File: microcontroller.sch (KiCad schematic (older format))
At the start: 12 parts

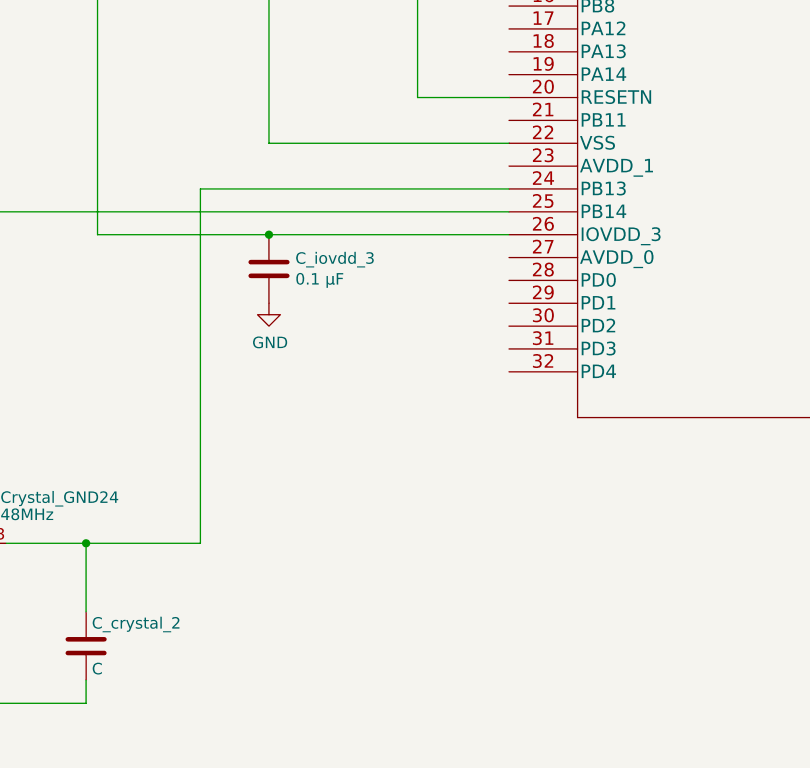
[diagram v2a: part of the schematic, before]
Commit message: Add avdd capacitors
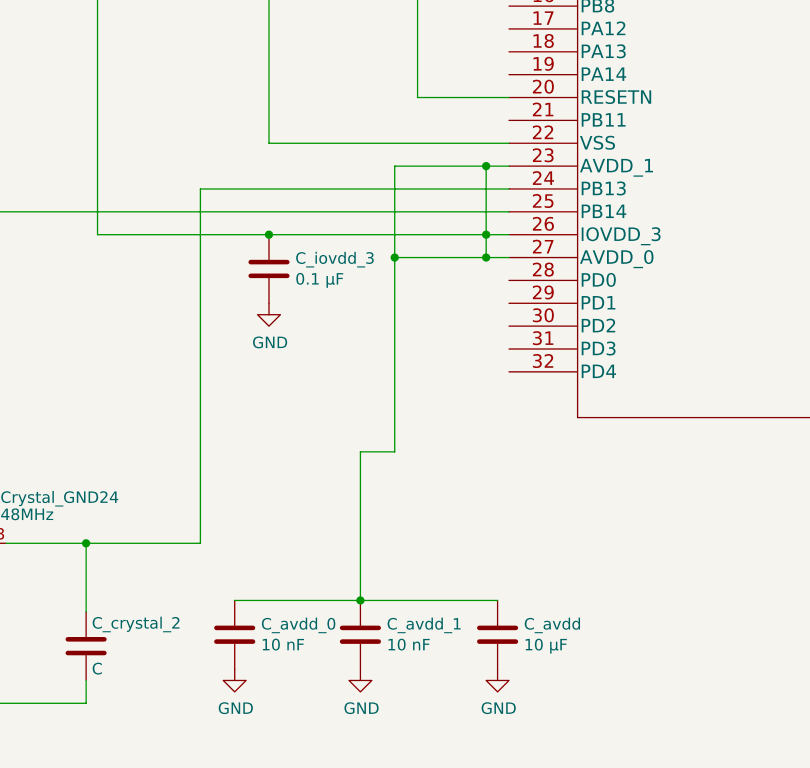
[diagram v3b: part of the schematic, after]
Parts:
- added C_avdd: 10 µF, symbol Device:C
- added C_avdd_0, C_avdd_1: 10 nF, symbol Device:C
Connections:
- net +3V3: now also U?.23 (AVDD_1), U?.27 (AVDD_0), C_avdd.1, C_avdd_0.1, C_avdd_1.1
- net GND: now also C_avdd.2, C_avdd_0.2, C_avdd_1.2
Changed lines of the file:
@@
 Connection ~ 3400 4750
 Wire Wire Line
-	3400 4750 4450 4750
+	3400 4750 4350 4750
 $Comp
 L power:GND #PWR?
@@
 	3150 1700 3150 2550
 Connection ~ 3150 2550
+Wire Wire Line
+	4450 4850 4350 4850
+Wire Wire Line
+	4350 4850 4350 4750
+Connection ~ 4350 4750
+Wire Wire Line
+	4350 4750 4450 4750
+Wire Wire Line
+	4450 4450 4350 4450
+Wire Wire Line
+	4350 4450 4350 4750
+Wire Wire Line
+	4350 4450 3950 4450
+Wire Wire Line
+	3950 4450 3950 4850
+Connection ~ 4350 4450
+Wire Wire Line
+	4350 4850 3950 4850
+Connection ~ 4350 4850
+$Comp
+L power:GND #PWR?
+U 1 1 5D8251E8
+P 3800 6650
+F 0 "#PWR?" H 3800 6400 50  0001 C CNN
+F 1 "GND" H 3805 6477 50  0000 C CNN
+F 2 "" H 3800 6650 50  0001 C CNN
+F 3 "" H 3800 6650 50  0001 C CNN
+	1    3800 6650
+	1    0    0    -1
+$EndComp
+Connection ~ 3800 6350
+$Comp
+L Device:C C_avdd_1
+U 1 1 5D824795
+P 3800 6500
+F 0 "C_avdd_1" H 3915 6546 50  0000 L CNN
+F 1 "10 nF" H 3915 6455 50  0000 L CNN
+F 2 "" H 3838 6350 50  0001 C CNN
+F 3 "~" H 3800 6500 50  0001 C CNN
+	1    3800 6500
+	1    0    0    -1
+$EndComp
+$Comp
+L power:GND #PWR?
+U 1 1 5D82344B
+P 3250 6650
+F 0 "#PWR?" H 3250 6400 50  0001 C CNN
+F 1 "GND" H 3255 6477 50  0000 C CNN
+F 2 "" H 3250 6650 50  0001 C CNN
+F 3 "" H 3250 6650 50  0001 C CNN
+	1    3250 6650
+	1    0    0    -1
+$EndComp
+Wire Wire Line
+	3800 5700 3800 6350
+Wire Wire Line
+	3800 6350 3250 6350
+$Comp
+L Device:C C_avdd_0
+U 1 1 5D81D35D
+P 3250 6500
+F 0 "C_avdd_0" H 3365 6546 50  0000 L CNN
+F 1 "10 nF" H 3365 6455 50  0000 L CNN
+F 2 "" H 3288 6350 50  0001 C CNN
+F 3 "~" H 3250 6500 50  0001 C CNN
+	1    3250 6500
+	1    0    0    -1
+$EndComp
+Wire Wire Line
+	3950 4850 3950 5700
+Wire Wire Line
+	3950 5700 3800 5700
+Connection ~ 3950 4850
+$Comp
+L Device:C C_avdd
+U 1 1 5D839716
+P 4400 6500
+F 0 "C_avdd" H 4515 6546 50  0000 L CNN
+F 1 "10 µF" H 4515 6455 50  0000 L CNN
+F 2 "" H 4438 6350 50  0001 C CNN
+F 3 "~" H 4400 6500 50  0001 C CNN
+	1    4400 6500
+	1    0    0    -1
+$EndComp
+$Comp
+L power:GND #PWR?
+U 1 1 5D83A872
+P 4400 6650
+F 0 "#PWR?" H 4400 6400 50  0001 C CNN
+F 1 "GND" H 4405 6477 50  0000 C CNN
+F 2 "" H 4400 6650 50  0001 C CNN
+F 3 "" H 4400 6650 50  0001 C CNN
+	1    4400 6650
+	1    0    0    -1
+$EndComp
+Wire Wire Line
+	4400 6350 3800 6350
 $EndSCHEMATC
